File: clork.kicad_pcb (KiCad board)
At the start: 2 copper layers, 25 x 37.5 mm, 34 parts, among them J1 UE27AC54100, J2 USB_B_Micro, M1 Stepper_Motor_unipolar_5pin, U1 RT9193-33GB, U2 STM32F103C8Tx, U3 ULN2003, Y1 8 Mhz, Y2 32.768 kHz

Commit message: Moved both USBs to bottom of board
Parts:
- removed the REF** at (116.8, 149.8)
- removed the REF** at (137.2, 116.8)
- added REF**: MountingHole_2.2mm_M2_DIN965_Pad, MountingHole:MountingHole_2.2mm_M2_DIN965_Pad, F.Cu at (115.2, 143.0)
- added REF**: MountingHole_2.2mm_M2_DIN965_Pad, MountingHole:MountingHole_2.2mm_M2_DIN965_Pad, F.Cu at (138.8, 116.8)
- moved J2 21.6 mm to (136.2, 149.2), turned to 0 degrees
- moved REF** 6.91 mm to (138.8, 143.0)
- moved J1 5.30 mm to (122.0, 147.0)
- moved REF** 1.50 mm to (115.2, 116.8)
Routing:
- net +5V: track 57.2 -> 79.7 mm
- net Net-(J2-Pad2): track 11.5 -> 17.8 mm
- net Net-(J2-Pad3): track 9.44 -> 13.8 mm
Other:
- board size 25 x 37.5 mm -> 28 x 37.5 mm

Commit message: Fixed PD resistors for BOOT0 and BOOT1
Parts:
- removed the REF** at (135.5, 127.2)
- added R6: 10k, Resistor_SMD:R_0603_1608Metric, B.Cu at (126.0, 132.7)
- R5: moved to B.Cu
- moved R5 7.25 mm to (128.2, 135.2)
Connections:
- R5 pad 1: +3V3 -> BOOT0
- R5 pad 2: Net-(R5-Pad2) -> GND
- U2 pad 20: Net-(U2-Pad20) -> BOOT1
- U2 pad 44: Net-(R5-Pad2) -> BOOT0
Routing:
- net +3V3: track 41.3 -> 37.3 mm, vias 5 -> 4
- net Net-(R5-Pad2): track 3.67 -> 0.00 mm
- net BOOT0: track 0.00 -> 2.52 mm, vias 0 -> 1
- net BOOT1: track 0.00 -> 2.40 mm, vias 0 -> 1
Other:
- board text added: "https://github.com/Wiles/clork Rev. 2"
- board text removed: "https://github.com/Wiles/clork Rev. 1"

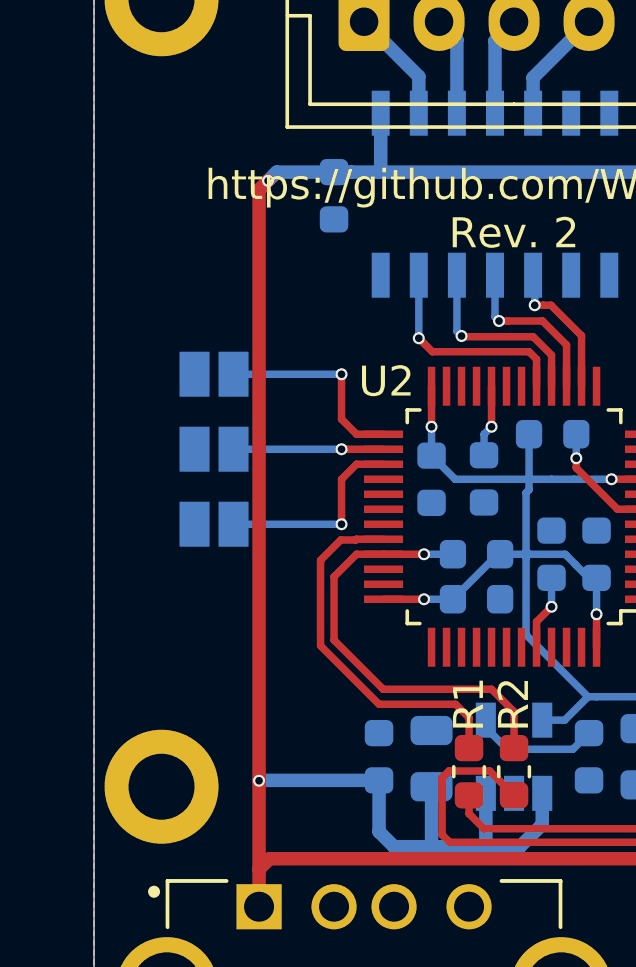
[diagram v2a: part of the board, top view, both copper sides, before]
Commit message: Added button for setting time
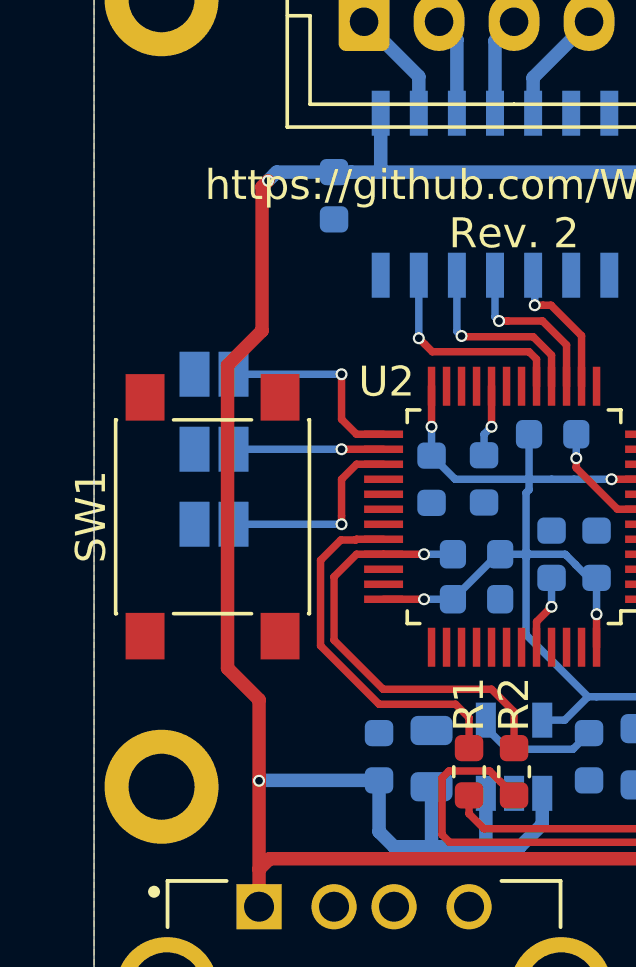
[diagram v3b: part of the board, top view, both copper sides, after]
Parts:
- added SW1: SW_Push, Button_Switch_SMD:SW_SPST_PTS645, F.Cu at (117.0, 134.0)
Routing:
- net +5V: track 79.7 -> 80.5 mm

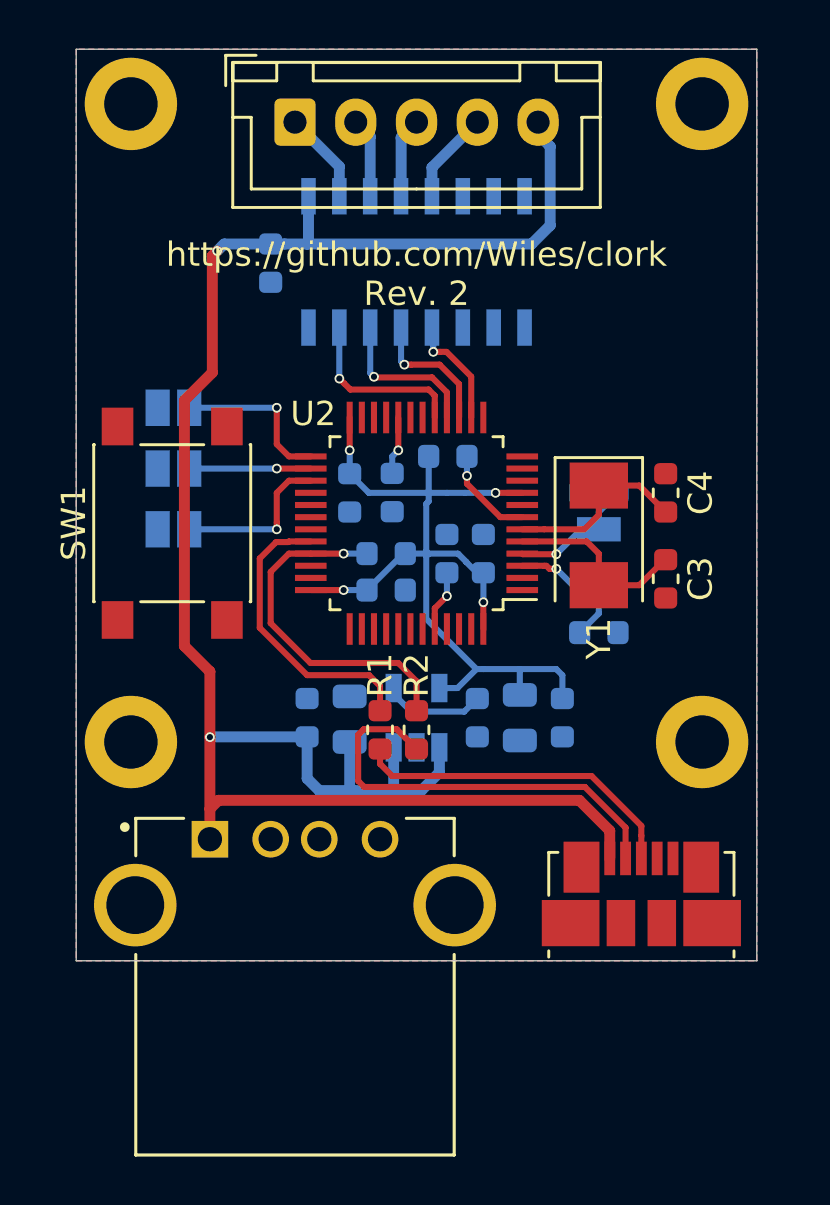
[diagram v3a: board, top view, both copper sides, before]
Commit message: Fixed reversed USB + and -
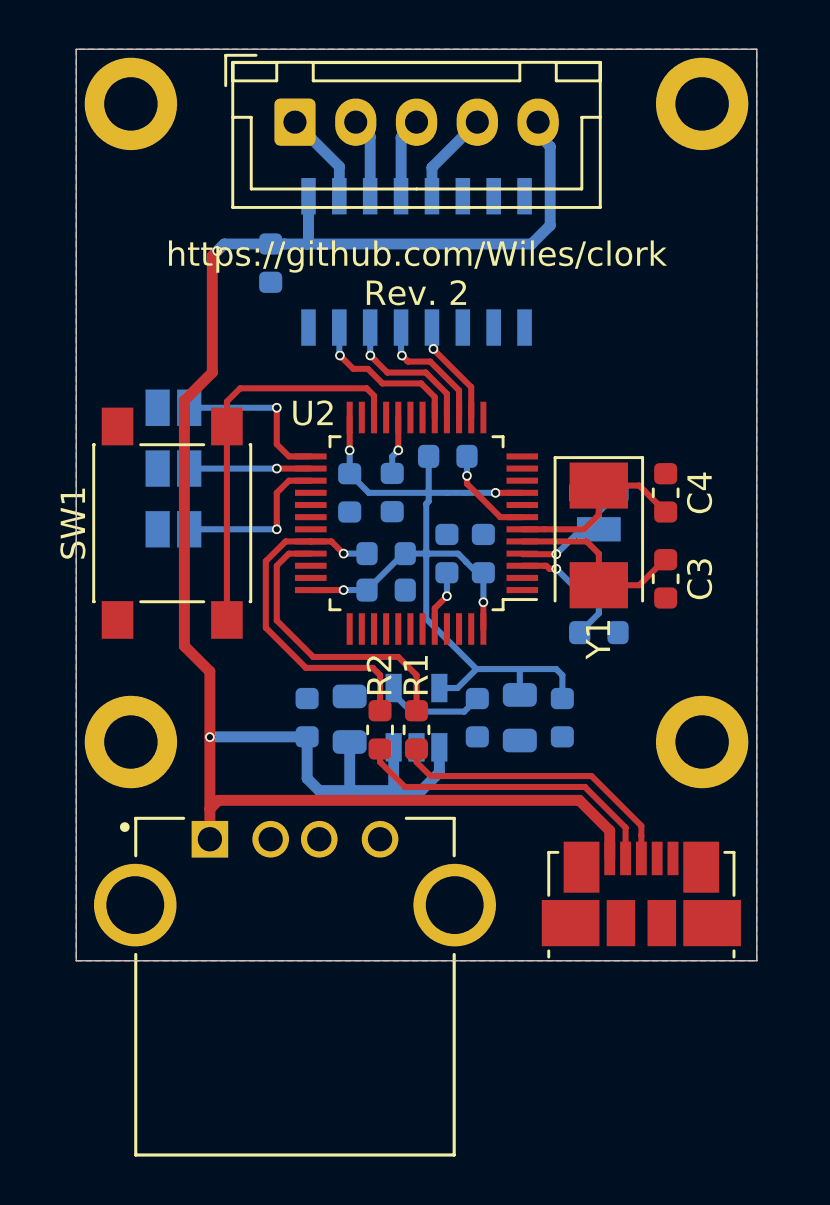
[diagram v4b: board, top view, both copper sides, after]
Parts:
- moved R1 1.50 mm to (127.0, 142.5)
- moved R2 1.50 mm to (125.5, 142.5)
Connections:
- U2 pad 32: USB+ -> USB-
- U2 pad 33: USB- -> USB+
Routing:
- net Net-(SW1-Pad2): track 0.00 -> 16.3 mm
- net Net-(J2-Pad2): track 17.8 -> 13.0 mm
- net Net-(J2-Pad3): track 13.8 -> 12.2 mm
- net Net-(U2-Pad17): track 7.21 -> 6.61 mm

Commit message: Fixed silkscreen
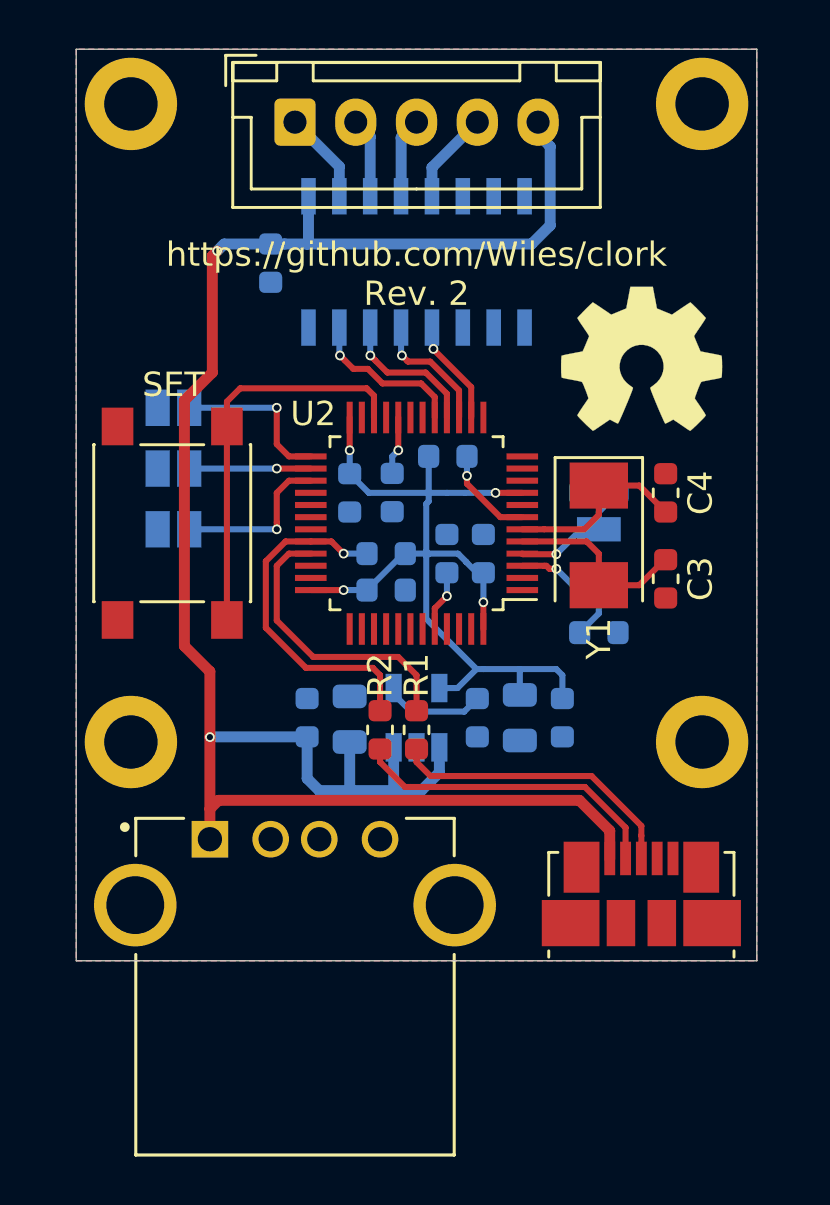
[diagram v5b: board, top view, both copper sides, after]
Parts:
- added REF**: OSHW-Symbol_6.7x6mm_SilkScreen, Symbol:OSHW-Symbol_6.7x6mm_SilkScreen, F.Cu at (136.2, 127.2)
- renumbered SW1 to SET
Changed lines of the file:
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@@
     (tracks 220)
     (zones 0)
-    (modules 35)
+    (modules 36)
     (nets 60)
   )
@@
     (tags "SPST Button Switch")
     (attr smd)
-    (fp_text reference SW1 (at 0 -4.05 90) (layer F.SilkS)
+    (fp_text reference SET (at 5.7 0.05 180) (layer F.SilkS)
       (effects (font (size 1 1) (thickness 0.15)))
     )
@@
     )
   )
+  (module Symbol:OSHW-Symbol_6.7x6mm_SilkScreen locked (layer F.Cu)
+    (at 136.25 127.25)
+    (descr "Open Source Hardware Symbol")
+    (tags "Logo Symbol OSHW")
+    (attr virtual)
+    (fp_text reference REF** (at 0 0) (layer F.SilkS) hide
+      (effects (font (size 1 1) (thickness 0.15)))
+    )
+    (fp_text value OSHW-Symbol_6.7x6mm_SilkScreen (at 0.75 0) (layer F.Fab) hide
+      (effects (font (size 1 1) (thickness 0.15)))
+    )
+    (fp_poly (pts (xy 0.555814 -2.531069) (xy 0.639635 -2.086445) (xy 0.94892 -1.958947) (xy 1.258206 -1.831449)
+      (xy 1.629246 -2.083754) (xy 1.733157 -2.154004) (xy 1.827087 -2.216728) (xy 1.906652 -2.269062)
+      (xy 1.96747 -2.308143) (xy 2.005157 -2.331107) (xy 2.015421 -2.336058) (xy 2.03391 -2.323324)
+      (xy 2.07342 -2.288118) (xy 2.129522 -2.234938) (xy 2.197787 -2.168282) (xy 2.273786 -2.092646)
+      (xy 2.353092 -2.012528) (xy 2.431275 -1.932426) (xy 2.503907 -1.856836) (xy 2.566559 -1.790255)
+      (xy 2.614803 -1.737182) (xy 2.64421 -1.702113) (xy 2.651241 -1.690377) (xy 2.641123 -1.66874)
+      (xy 2.612759 -1.621338) (xy 2.569129 -1.552807) (xy 2.513218 -1.467785) (xy 2.448006 -1.370907)
+      (xy 2.410219 -1.31565) (xy 2.341343 -1.214752) (xy 2.28014 -1.123701) (xy 2.229578 -1.04703)
+      (xy 2.192628 -0.989272) (xy 2.172258 -0.954957) (xy 2.169197 -0.947746) (xy 2.176136 -0.927252)
+      (xy 2.195051 -0.879487) (xy 2.223087 -0.811168) (xy 2.257391 -0.729011) (xy 2.295109 -0.63973)
+      (xy 2.333387 -0.550042) (xy 2.36937 -0.466662) (xy 2.400206 -0.396306) (xy 2.423039 -0.34569)
+      (xy 2.435017 -0.321529) (xy 2.435724 -0.320578) (xy 2.454531 -0.315964) (xy 2.504618 -0.305672)
+      (xy 2.580793 -0.290713) (xy 2.677865 -0.272099) (xy 2.790643 -0.250841) (xy 2.856442 -0.238582)
+      (xy 2.97695 -0.215638) (xy 3.085797 -0.193805) (xy 3.177476 -0.174278) (xy 3.246481 -0.158252)
+      (xy 3.287304 -0.146921) (xy 3.295511 -0.143326) (xy 3.303548 -0.118994) (xy 3.310033 -0.064041)
+      (xy 3.31497 0.015108) (xy 3.318364 0.112026) (xy 3.320218 0.220287) (xy 3.320538 0.333465)
+      (xy 3.319327 0.445135) (xy 3.31659 0.548868) (xy 3.312331 0.638241) (xy 3.306555 0.706826)
+      (xy 3.299267 0.748197) (xy 3.294895 0.75681) (xy 3.268764 0.767133) (xy 3.213393 0.781892)
+      (xy 3.136107 0.799352) (xy 3.04423 0.81778) (xy 3.012158 0.823741) (xy 2.857524 0.852066)
+      (xy 2.735375 0.874876) (xy 2.641673 0.89308) (xy 2.572384 0.907583) (xy 2.523471 0.919292)
+      (xy 2.490897 0.929115) (xy 2.470628 0.937956) (xy 2.458626 0.946724) (xy 2.456947 0.948457)
+      (xy 2.440184 0.976371) (xy 2.414614 1.030695) (xy 2.382788 1.104777) (xy 2.34726 1.191965)
+      (xy 2.310583 1.285608) (xy 2.275311 1.379052) (xy 2.243996 1.465647) (xy 2.219193 1.53874)
+      (xy 2.203454 1.591678) (xy 2.199332 1.617811) (xy 2.199676 1.618726) (xy 2.213641 1.640086)
+      (xy 2.245322 1.687084) (xy 2.291391 1.754827) (xy 2.348518 1.838423) (xy 2.413373 1.932982)
+      (xy 2.431843 1.959854) (xy 2.497699 2.057275) (xy 2.55565 2.146163) (xy 2.602538 2.221412)
+      (xy 2.635207 2.27792) (xy 2.6505 2.310581) (xy 2.651241 2.314593) (xy 2.638392 2.335684)
+      (xy 2.602888 2.377464) (xy 2.549293 2.435445) (xy 2.482171 2.505135) (xy 2.406087 2.582045)
+      (xy 2.325604 2.661683) (xy 2.245287 2.739561) (xy 2.169699 2.811186) (xy 2.103405 2.87207)
+      (xy 2.050969 2.917721) (xy 2.016955 2.94365) (xy 2.007545 2.947883) (xy 1.985643 2.937912)
+      (xy 1.9408 2.91102) (xy 1.880321 2.871736) (xy 1.833789 2.840117) (xy 1.749475 2.782098)
+      (xy 1.649626 2.713784) (xy 1.549473 2.645579) (xy 1.495627 2.609075) (xy 1.313371 2.4858)
+      (xy 1.160381 2.56852) (xy 1.090682 2.604759) (xy 1.031414 2.632926) (xy 0.991311 2.648991)
+      (xy 0.981103 2.651226) (xy 0.968829 2.634722) (xy 0.944613 2.588082) (xy 0.910263 2.515609)
+      (xy 0.867588 2.421606) (xy 0.818394 2.310374) (xy 0.76449 2.186215) (xy 0.707684 2.053432)
+      (xy 0.649782 1.916327) (xy 0.592593 1.779202) (xy 0.537924 1.646358) (xy 0.487584 1.522098)
+      (xy 0.44338 1.410725) (xy 0.407119 1.316539) (xy 0.380609 1.243844) (xy 0.365658 1.196941)
+      (xy 0.363254 1.180833) (xy 0.382311 1.160286) (xy 0.424036 1.126933) (xy 0.479706 1.087702)
+      (xy 0.484378 1.084599) (xy 0.628264 0.969423) (xy 0.744283 0.835053) (xy 0.83143 0.685784)
+      (xy 0.888699 0.525913) (xy 0.915086 0.359737) (xy 0.909585 0.191552) (xy 0.87119 0.025655)
+      (xy 0.798895 -0.133658) (xy 0.777626 -0.168513) (xy 0.666996 -0.309263) (xy 0.536302 -0.422286)
+      (xy 0.390064 -0.506997) (xy 0.232808 -0.562806) (xy 0.069057 -0.589126) (xy -0.096667 -0.58537)
+      (xy -0.259838 -0.55095) (xy -0.415935 -0.485277) (xy -0.560433 -0.387765) (xy -0.605131 -0.348187)
+      (xy -0.718888 -0.224297) (xy -0.801782 -0.093876) (xy -0.858644 0.052315) (xy -0.890313 0.197088)
+      (xy -0.898131 0.35986) (xy -0.872062 0.52344) (xy -0.814755 0.682298) (xy -0.728856 0.830906)
+      (xy -0.617014 0.963735) (xy -0.481877 1.075256) (xy -0.464117 1.087011) (xy -0.40785 1.125508)
+      (xy -0.365077 1.158863) (xy -0.344628 1.18016) (xy -0.344331 1.180833) (xy -0.348721 1.203871)
+      (xy -0.366124 1.256157) (xy -0.394732 1.33339) (xy -0.432735 1.431268) (xy -0.478326 1.545491)
+      (xy -0.529697 1.671758) (xy -0.585038 1.805767) (xy -0.642542 1.943218) (xy -0.700399 2.079808)
+      (xy -0.756802 2.211237) (xy -0.809942 2.333205) (xy -0.85801 2.441409) (xy -0.899199 2.531549)
+      (xy -0.931699 2.599323) (xy -0.953703 2.64043) (xy -0.962564 2.651226) (xy -0.98964 2.642819)
+      (xy -1.040303 2.620272) (xy -1.105817 2.587613) (xy -1.141841 2.56852) (xy -1.294832 2.4858)
+      (xy -1.477088 2.609075) (xy -1.570125 2.672228) (xy -1.671985 2.741727) (xy -1.767438 2.807165)
+      (xy -1.81525 2.840117) (xy -1.882495 2.885273) (xy -1.939436 2.921057) (xy -1.978646 2.942938)
+      (xy -1.991381 2.947563) (xy -2.009917 2.935085) (xy -2.050941 2.900252) (xy -2.110475 2.846678)
+      (xy -2.184542 2.777983) (xy -2.269165 2.697781) (xy -2.322685 2.646286) (xy -2.416319 2.554286)
+      (xy -2.497241 2.471999) (xy -2.562177 2.402945) (xy -2.607858 2.350644) (xy -2.631011 2.318616)
+      (xy -2.633232 2.312116) (xy -2.622924 2.287394) (xy -2.594439 2.237405) (xy -2.550937 2.167212)
+      (xy -2.495577 2.081875) (xy -2.43152 1.986456) (xy -2.413303 1.959854) (xy -2.346927 1.863167)
+      (xy -2.287378 1.776117) (xy -2.237984 1.703595) (xy -2.202075 1.650493) (xy -2.182981 1.621703)
+      (xy -2.181136 1.618726) (xy -2.183895 1.595782) (xy -2.198538 1.545336) (xy -2.222513 1.474041)
+      (xy -2.253266 1.388547) (xy -2.288244 1.295507) (xy -2.324893 1.201574) (xy -2.360661 1.113399)
+      (xy -2.392994 1.037634) (xy -2.419338 0.980931) (xy -2.437142 0.949943) (xy -2.438407 0.948457)
+      (xy -2.449294 0.939601) (xy -2.467682 0.930843) (xy -2.497606 0.921277) (xy -2.543103 0.909996)
+      (xy -2.608209 0.896093) (xy -2.696961 0.878663) (xy -2.813393 0.856798) (xy -2.961542 0.829591)
+      (xy -2.993618 0.823741) (xy -3.088686 0.805374) (xy -3.171565 0.787405) (xy -3.23493 0.771569)
+      (xy -3.271458 0.7596) (xy -3.276356 0.75681) (xy -3.284427 0.732072) (xy -3.290987 0.67679)
+      (xy -3.296033 0.597389) (xy -3.299559 0.500296) (xy -3.301561 0.391938) (xy -3.302036 0.27874)
+      (xy -3.300977 0.167128) (xy -3.298382 0.063529) (xy -3.294246 -0.025632) (xy -3.288563 -0.093928)
+      (xy -3.281331 -0.134934) (xy -3.276971 -0.143326) (xy -3.252698 -0.151792) (xy -3.197426 -0.165565)
+      (xy -3.116662 -0.18345) (xy -3.015912 -0.204252) (xy -2.900683 -0.226777) (xy -2.837902 -0.238582)
+      (xy -2.718787 -0.260849) (xy -2.612565 -0.281021) (xy -2.524427 -0.298085) (xy -2.459566 -0.311031)
+      (xy -2.423174 -0.318845) (xy -2.417184 -0.320578) (xy -2.407061 -0.34011) (xy -2.385662 -0.387157)
+      (xy -2.355839 -0.454997) (xy -2.320445 -0.536909) (xy -2.282332 -0.626172) (xy -2.244353 -0.716065)
+      (xy -2.20936 -0.799865) (xy -2.180206 -0.870853) (xy -2.159743 -0.922306) (xy -2.150823 -0.947503)
+      (xy -2.150657 -0.948604) (xy -2.160769 -0.968481) (xy -2.189117 -1.014223) (xy -2.232723 -1.081283)
+      (xy -2.288606 -1.165116) (xy -2.353787 -1.261174) (xy -2.391679 -1.31635) (xy -2.460725 -1.417519)
+      (xy -2.52205 -1.50937) (xy -2.572663 -1.587256) (xy -2.609571 -1.646531) (xy -2.629782 -1.682549)
+      (xy -2.632701 -1.690623) (xy -2.620153 -1.709416) (xy -2.585463 -1.749543) (xy -2.533063 -1.806507)
+      (xy -2.467384 -1.875815) (xy -2.392856 -1.952969) (xy -2.313913 -2.033475) (xy -2.234983 -2.112837)
+      (xy -2.1605 -2.18656) (xy -2.094894 -2.250148) (xy -2.042596 -2.299106) (xy -2.008039 -2.328939)
+      (xy -1.996478 -2.336058) (xy -1.977654 -2.326047) (xy -1.932631 -2.297922) (xy -1.865787 -2.254546)
+      (xy -1.781499 -2.198782) (xy -1.684144 -2.133494) (xy -1.610707 -2.083754) (xy -1.239667 -1.831449)
+      (xy -0.621095 -2.086445) (xy -0.537275 -2.531069) (xy -0.453454 -2.975693) (xy 0.471994 -2.975693)
+      (xy 0.555814 -2.531069)) (layer F.SilkS) (width 0.01))
+  )
   (gr_text "https://github.com/Wiles/clork\nRev. 2" (at 127 123.75) (layer F.SilkS)
